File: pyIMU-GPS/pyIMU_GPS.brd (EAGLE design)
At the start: 40.6 x 33 mm, 37 parts, among them J3 22-27-2031-03, J4 BU-SMA-V, U1 BMP180, U2 MPU-9150, U3 FGPMMOPA6H, U5 MAX4173, U6 MCP1802, U7 MCP601OT

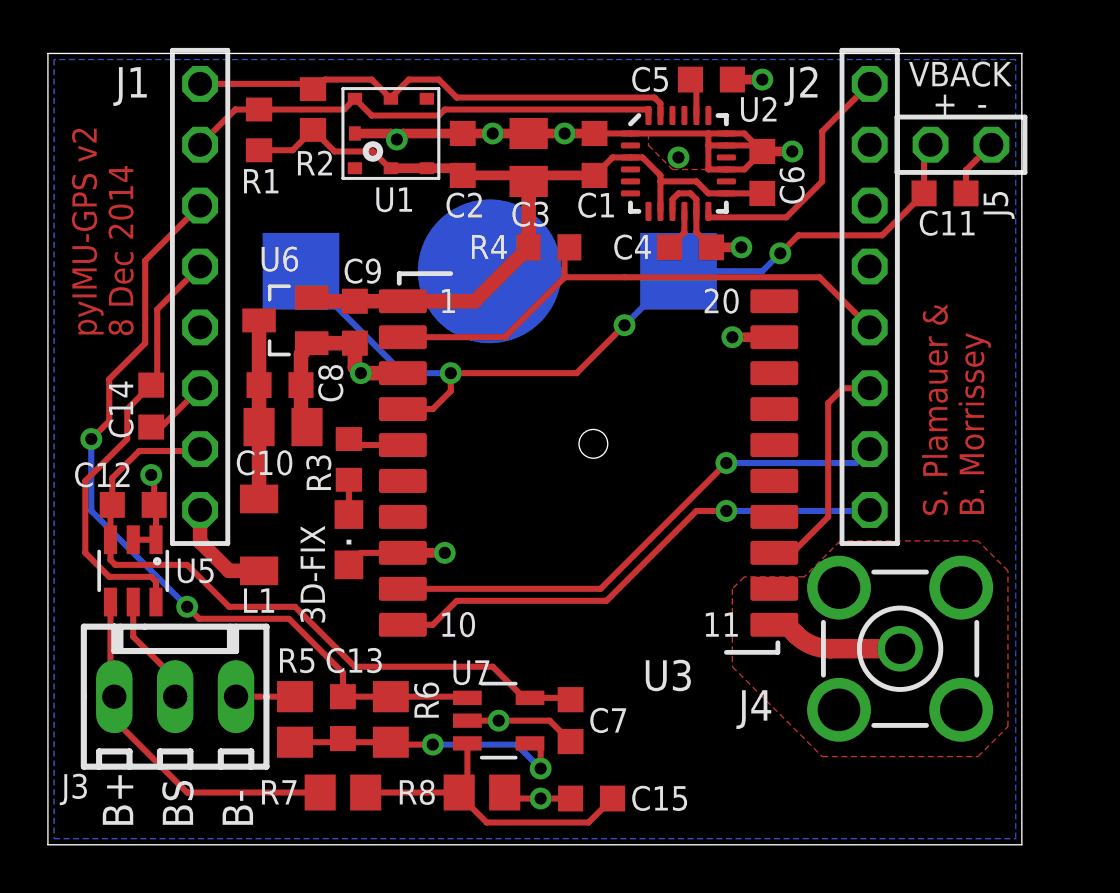
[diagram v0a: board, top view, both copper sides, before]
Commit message: Add mounting hole to board, move MPU_INT from XY8 to XY5, enlarge board slightly, shift GPS module and some other small changes
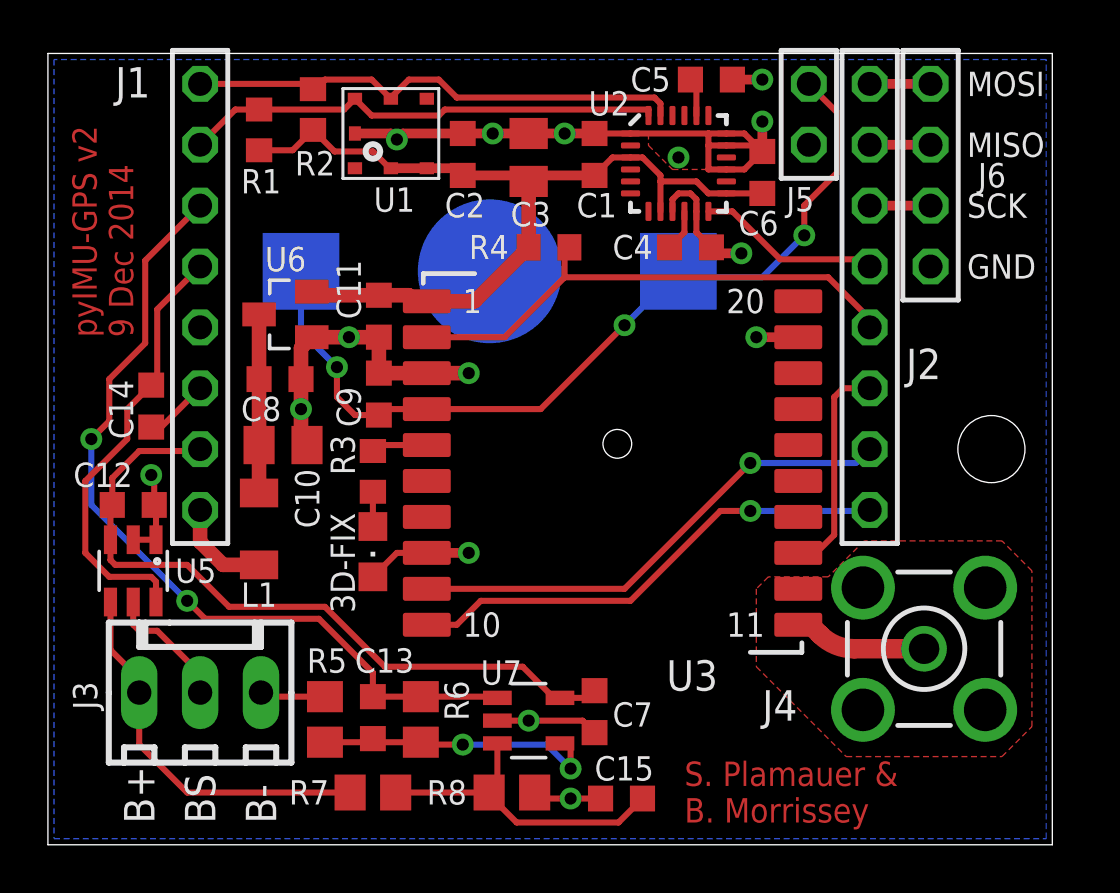
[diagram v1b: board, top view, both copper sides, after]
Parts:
- added J6: (no value), pyIMU_GPS:TSW-104-S-S-MOD
- moved C11 24.2 mm to (10.0, 10.6), turned to 270 degrees
- moved J5 6.48 mm to (27.9, 19.1), turned to 270 degrees
- moved C9 3.16 mm to (10.0, 7.38), turned to 90 degrees
- moved C13 1.25 mm to (9.75, -6.12)
- moved C15 1.25 mm to (20.1, -9.50)
- moved R5 1.25 mm to (7.75, -6.20)
- moved R6 1.25 mm to (11.8, -6.20)
- moved R7 1.25 mm to (9.75, -9.25)
- moved R8 1.25 mm to (15.6, -9.25)
- moved U7 1.25 mm to (16.2, -6.25)
- moved 3D-FIX 1.12 mm to (9.75, 0.80)
- moved R3 1.12 mm to (9.75, 4.15)
- moved C7 1.07 mm to (19.0, -5.88)
- moved J3 1.05 mm to (2.54, -5.08)
- moved J4 1.00 mm to (32.8, -3.25)
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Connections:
- removed net XY-5: J2.5
- removed net XY-8/MPU_INT: J2.8, U2.12
- new net XY-5/MPU_INT: J2.5, U2.12
- new net XY-8: J2.8, J6.1
- net 3V3: now also C11.1; no longer C9.1
- net GND: now also J6.4
- net VBACK: now also C9.1; no longer C11.1
- net XY-6: now also J6.3
- net XY-7: now also J6.2
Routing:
- net XY-8/MPU_INT: track 10.5 -> 0.00 mm
- net XY-5/MPU_INT: track 0.00 -> 7.68 mm
- net XY-8: track 0.00 -> 2.54 mm
- net XY-7: track 0.00 -> 2.54 mm
- net XY-6: track 0.00 -> 2.54 mm
- net GND: track 62.4 -> 64.0 mm, vias 13 -> 15
- net B+: track 14.8 -> 16.1 mm
- net XY-11/ADC: track 34.1 -> 35.2 mm
- net 3V3-PYB: track 29.2 -> 30.3 mm
- net XY-2/RX: track 21.9 -> 20.9 mm
- net XY-1/TX: track 21.5 -> 20.5 mm
- net VBACK: track 36.1 -> 37.0 mm
- net XY-4/GPS_!RESET: track 22.7 -> 21.9 mm
- net BS: track 4.67 -> 5.37 mm
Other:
- board size 40.6 x 33 mm -> 41.9 x 33 mm
- board text added: "GND"
- board text added: "MISO"
- board text added: "MOSI"
- board text added: "SCK"
- board text added: "pyIMU-GPS v2 9 Dec 2014"
- board text removed: "VBACK + -"
- board text removed: "pyIMU-GPS v2 8 Dec 2014"

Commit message: Fix GPS module package so that all silkscreen markings are in top silkscreen layer Add a via in the SMA antenna ground pour. Move via in VBACK trace outside of battery holder outline to prevent possible short circuit. Revise date (10 December 2014) Correct battery voltage measurement calculation in schematic text.
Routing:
- net VBACK: track 37.0 -> 38.3 mm
- net GND: vias 15 -> 16
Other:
- board text added: "pyIMU-GPS v2 10 Dec 2014"
- board text removed: "pyIMU-GPS v2 9 Dec 2014"
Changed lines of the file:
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@@
 <layer number="20" name="Dimension" color="15" fill="1" visible="yes" active="yes"/>
 <layer number="21" name="tPlace" color="7" fill="1" visible="yes" active="yes"/>
-<layer number="22" name="bPlace" color="7" fill="1" visible="yes" active="yes"/>
+<layer number="22" name="bPlace" color="7" fill="1" visible="no" active="yes"/>
 <layer number="23" name="tOrigins" color="15" fill="1" visible="yes" active="yes"/>
 <layer number="24" name="bOrigins" color="15" fill="1" visible="yes" active="yes"/>
@@
 <text x="3.175" y="-10.541" size="1.27" layer="21" ratio="10" rot="R90">BS</text>
 <text x="5.715" y="-10.541" size="1.27" layer="21" ratio="10" rot="R90">B-</text>
-<text x="-0.25" y="9.75" size="1.016" layer="1" font="vector" ratio="15" rot="R90">pyIMU-GPS v2
-9 Dec 2014</text>
+<text x="-0.25" y="9.5" size="1.016" layer="1" font="vector" ratio="15" rot="R90">pyIMU-GPS v2
+10 Dec 2014</text>
 <hole x="35.56" y="5.08" drill="2.8"/>
 <text x="34.544" y="19.812" size="1.016" layer="21" ratio="10">MOSI</text>
@@
 <wire x1="18.5" y1="-6.25" x2="16.25" y2="-6.25" width="0.254" layer="1"/>
 <contactref element="J6" pad="4"/>
+<via x="27.5" y="-4.25" extent="1-16" drill="0.508"/>
 </signal>
 <signal name="XY-8">
@@
 <contactref element="B1" pad="+@1"/>
 <contactref element="B1" pad="+@2"/>
-<wire x1="16.75" y1="6.75" x2="20.25" y2="10.25" width="0.254" layer="1"/>
-<wire x1="20.25" y1="10.25" x2="22.5" y2="12.5" width="0.254" layer="16"/>
-<via x="20.25" y="10.25" extent="1-16" drill="0.508"/>
+<wire x1="19" y1="6.75" x2="22.5" y2="10.25" width="0.254" layer="1"/>
+<wire x1="22.5" y1="10.25" x2="22.5" y2="12.5" width="0.254" layer="16"/>
+<via x="22.5" y="10.25" extent="1-16" drill="0.508"/>
 <wire x1="22.5" y1="12.5" x2="22.75" y2="12.25" width="0.254" layer="16"/>
 <wire x1="22.75" y1="12.25" x2="26" y2="12.25" width="0.254" layer="16"/>
@@
 <wire x1="9" y1="6.5" x2="8.25" y2="7.25" width="0.254" layer="1"/>
 <wire x1="8.25" y1="7.25" x2="8.25" y2="8.5" width="0.254" layer="1"/>
-<wire x1="16.75" y1="6.75" x2="11.5" y2="6.75" width="0.254" layer="1"/>
+<wire x1="19" y1="6.75" x2="11.5" y2="6.75" width="0.254" layer="1"/>
 <wire x1="6.75" y1="12.5" x2="6.75" y2="10" width="0.254" layer="16"/>
 <wire x1="6.75" y1="10" x2="8.25" y2="8.5" width="0.254" layer="16"/>

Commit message: Enlarge signal feed hole in center of SMA connector footprint. Available parts probably would not have fit if boards were run with previous footprint.
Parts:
- J4: device con-coax:BU-SMA-V -> pyIMU_GPS:BU-SMA-V
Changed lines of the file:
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@@
 <attribute name="NAME" x="22" y="-5" size="1.27" layer="21"/>
 </element>
-<element name="J4" library="con-coax" package="BU-SMA-V" value="BU-SMA-V" x="32.75" y="-3.25" smashed="yes" rot="R90">
+<element name="J4" library="pyIMU_GPS" package="BU-SMA-V" value="BU-SMA-V" x="32.75" y="-3.25" smashed="yes" rot="R90">
 <attribute name="OC_NEWARK" value="unknown" x="32.75" y="-3.25" size="1.016" layer="27" ratio="10" rot="R90" display="off"/>
 <attribute name="MPN" value="" x="32.75" y="-3.25" size="1.016" layer="27" ratio="10" rot="R90" display="off"/>
